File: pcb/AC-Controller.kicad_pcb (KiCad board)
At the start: 2 copper layers, 66 x 67 mm, 69 parts, among them J1 Serial, J2 USB_C_Top, J3 USB_C_Bottom, Q1 2N7002, Q2 AO3401A, SW1 Mode, SW2 Value, U1 ESP32-WROOM-32, U2 TPS63000, U3 TPS63000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

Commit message: style: schematics cleanup
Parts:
- R24, R25: value 1M -> 10M
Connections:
- net VBUS renamed /Power/V_{BUS}
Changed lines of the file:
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@@
   )
   (paper "A4")
+  (title_block
+    (title "Qeteshs AC-Controller")
+    (date "~DATE~")
+    (rev "~VERSION~")
+  )
   (layers
     (0 "F.Cu" signal)
@@
   (net 5 "/Encoder1_A")
   (net 6 "/Encoder2_A")
-  (net 7 "VBUS")
+  (net 7 "/Power/V_{BUS}")
   (net 8 "Net-(D1-A)")
   (net 9 "/LCD_VO")
@@
     (descr "Resistor SMD 0402 (1005 Metric), square (rectangular) end terminal, IPC_7351 nominal, (Body size source: IPC-SM-782 page 72, https://www.pcb-3d.com/wordpress/wp-content/uploads/ipc-sm-782a_amendment_1_and_2.pdf), generated with kicad-footprint-generator")
     (tags "resistor")
-    (property "LCSC" "C26083")
+    (property "LCSC" "C26082")
     (property "Sheetfile" "AC-Controller.kicad_sch")
     (property "Sheetname" "")
@@
         (effects (font (size 0.8 0.8) (thickness 0.15)))
     )
-    (fp_text value "1M" (at 0 1.17) (layer "F.Fab")
+    (fp_text value "10M" (at 0 1.17) (layer "F.Fab")
         (effects (font (size 1 1) (thickness 0.15)))
     )
@@
       (stroke (width 0.1) (type solid)) (layer "F.Fab"))
     (pad "1" smd roundrect (at -0.9375 -0.95 270) (size 1.475 0.6) (layers "F.Cu" "F.Paste" "F.Mask") (roundrect_rratio 0.25)
-      (net 7 "VBUS") (pinfunction "G") (pintype "input"))
+      (net 7 "/Power/V_{BUS}") (pinfunction "G") (pintype "input"))
     (pad "2" smd roundrect (at -0.9375 0.95 270) (size 1.475 0.6) (layers "F.Cu" "F.Paste" "F.Mask") (roundrect_rratio 0.25)
       (net 43 "/Power/V_{IN}") (pinfunction "S") (pintype "passive"))
@@
       (net 39 "/Power/CC1a") (pinfunction "CC1") (pintype "bidirectional"))
     (pad "A9" smd rect (at 1.52 -3.08 180) (size 0.76 1.2) (layers "F.Cu" "F.Paste" "F.Mask")
-      (net 7 "VBUS") (pinfunction "VBUS") (pintype "passive"))
+      (net 7 "/Power/V_{BUS}") (pinfunction "VBUS") (pintype "passive"))
     (pad "A12" smd rect (at 2.75 -3.08 180) (size 0.8 1.2) (layers "F.Cu" "F.Paste" "F.Mask")
       (net 1 "GND") (pinfunction "GND") (pintype "passive"))
@@
       (net 40 "/Power/CC2a") (pinfunction "CC2") (pintype "bidirectional"))
     (pad "B9" smd rect (at -1.52 -3.08 180) (size 0.76 1.2) (layers "F.Cu" "F.Paste" "F.Mask")
-      (net 7 "VBUS") (pinfunction "VBUS") (pintype "passive"))
+      (net 7 "/Power/V_{BUS}") (pinfunction "VBUS") (pintype "passive"))
     (pad "B12" smd rect (at -2.75 -3.08 180) (size 0.8 1.2) (layers "F.Cu" "F.Paste" "F.Mask")
       (net 1 "GND") (pinfunction "GND") (pintype "passive"))
@@
       (stroke (width 0.1) (type solid)) (layer "F.Fab"))
     (pad "1" smd roundrect (at -0.51 0 270) (size 0.54 0.64) (layers "F.Cu" "F.Paste" "F.Mask") (roundrect_rratio 0.25)
-      (net 7 "VBUS") (pintype "passive"))
+      (net 7 "/Power/V_{BUS}") (pintype "passive"))
     (pad "2" smd roundrect (at 0.51 0 270) (size 0.54 0.64) (layers "F.Cu" "F.Paste" "F.Mask") (roundrect_rratio 0.25)
       (net 1 "GND") (pintype "passive"))
@@
       (net 43 "/Power/V_{IN}") (pinfunction "K") (pintype "passive"))
     (pad "2" smd roundrect (at 1.05 0) (size 0.6 0.45) (layers "F.Cu" "F.Paste" "F.Mask") (roundrect_rratio 0.25)
-      (net 7 "VBUS") (pinfunction "A") (pintype "passive"))
+      (net 7 "/Power/V_{BUS}") (pinfunction "A") (pintype "passive"))
     (model "${KICAD6_3DMODEL_DIR}/Diode_SMD.3dshapes/D_SOD-323.wrl"
       (offset (xyz 0 0 0))
@@
       (net 41 "/Power/CC1b") (pinfunction "CC1") (pintype "bidirectional"))
     (pad "A9" smd rect (at 1.52 -3.08) (size 0.76 1.2) (layers "F.Cu" "F.Paste" "F.Mask")
-      (net 7 "VBUS") (pinfunction "VBUS") (pintype "passive"))
+      (net 7 "/Power/V_{BUS}") (pinfunction "VBUS") (pintype "passive"))
     (pad "A12" smd rect (at 2.75 -3.08) (size 0.8 1.2) (layers "F.Cu" "F.Paste" "F.Mask")
       (net 1 "GND") (pinfunction "GND") (pintype "passive"))
@@
       (net 42 "/Power/CC2b") (pinfunction "CC2") (pintype "bidirectional"))
     (pad "B9" smd rect (at -1.52 -3.08) (size 0.76 1.2) (layers "F.Cu" "F.Paste" "F.Mask")
-      (net 7 "VBUS") (pinfunction "VBUS") (pintype "passive"))
+      (net 7 "/Power/V_{BUS}") (pinfunction "VBUS") (pintype "passive"))
     (pad "B12" smd rect (at -2.75 -3.08) (size 0.8 1.2) (layers "F.Cu" "F.Paste" "F.Mask")
       (net 1 "GND") (pinfunction "GND") (pintype "passive"))
@@
       (net 1 "GND") (pinfunction "GND") (pintype "power_in"))
     (pad "4" smd roundrect (at -2.475 1.905) (size 1.97 0.6) (layers "F.Cu" "F.Paste" "F.Mask") (roundrect_rratio 0.07)
-      (net 7 "VBUS") (pinfunction "VCC") (pintype "power_in"))
+      (net 7 "/Power/V_{BUS}") (pinfunction "VCC") (pintype "power_in"))
     (pad "5" smd roundrect (at 2.475 1.905) (size 1.97 0.6) (layers "F.Cu" "F.Paste" "F.Mask") (roundrect_rratio 0.07)
       (net 55 "/Battery+") (pinfunction "BAT") (pintype "output"))
@@
       (net 53 "/~{Battery_Charging}") (pinfunction "~{CHRG}") (pintype "output"))
     (pad "8" smd roundrect (at 2.475 -1.905) (size 1.97 0.6) (layers "F.Cu" "F.Paste" "F.Mask") (roundrect_rratio 0.07)
-      (net 7 "VBUS") (pinfunction "CE") (pintype "input"))
+      (net 7 "/Power/V_{BUS}") (pinfunction "CE") (pintype "input"))
     (pad "9" smd rect (at 0 0) (size 2.413 3.302) (layers "F.Cu" "F.Mask")
       (net 1 "GND") (pinfunction "EP") (pintype "passive"))
@@
     (descr "Resistor SMD 0402 (1005 Metric), square (rectangular) end terminal, IPC_7351 nominal, (Body size source: IPC-SM-782 page 72, https://www.pcb-3d.com/wordpress/wp-content/uploads/ipc-sm-782a_amendment_1_and_2.pdf), generated with kicad-footprint-generator")
     (tags "resistor")
-    (property "LCSC" "C26083")
+    (property "LCSC" "C26082")
     (property "Sheetfile" "AC-Controller.kicad_sch")
     (property "Sheetname" "")
@@
         (effects (font (size 0.8 0.8) (thickness 0.15)))
     )
-    (fp_text value "1M" (at 0 3.17) (layer "F.Fab")
+    (fp_text value "10M" (at 0 3.17) (layer "F.Fab")
         (effects (font (size 1 1) (thickness 0.15)))
     )
@@
     )
   )
-  (zone (net 7) (net_name "VBUS") (layer "B.Cu") (name "VBUS") (hatch edge 0.5)
+  (zone (net 7) (net_name "/Power/V_{BUS}") (layer "B.Cu") (name "VBUS") (hatch edge 0.5)
     (priority 10)
     (connect_pads (clearance 0.25))

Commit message: style: use correct variables
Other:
- board text added: "${VERSION} ${DATE}"
- board text removed: "~VERSION~ ~DATE~"
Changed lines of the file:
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@@
   (title_block
     (title "Qeteshs AC-Controller")
-    (date "~DATE~")
-    (rev "~VERSION~")
+    (date "${DATE}")
+    (rev "${VERSION}")
   )
   (layers
@@
     (effects (font (size 1 1) (thickness 0.15)) (justify bottom mirror))
   )
-  (gr_text "~VERSION~\n~DATE~" (at 150 95.75) (layer "B.SilkS")
+  (gr_text "${VERSION}\n${DATE}" (at 150 95.75) (layer "B.SilkS")
     (effects (font (size 1 1) (thickness 0.15)) (justify mirror))
   )
@@
     (effects (font (size 1 1) (thickness 0.15)) (justify right mirror))
   )
-  (gr_text "~VERSION~\n~DATE~" (at 150 66.75) (layer "F.SilkS")
+  (gr_text "${VERSION}\n${DATE}" (at 150 66.75) (layer "F.SilkS")
     (effects (font (size 1 1) (thickness 0.15)))
   )

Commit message: style: add 3d models for pcb render
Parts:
- L1, L2: value 3.3uH -> DR74-3R3-R
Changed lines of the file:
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@@
         (effects (font (size 0.8 0.8) (thickness 0.15)))
     )
-    (fp_text value "3.3uH" (at 0 -4.75 unlocked) (layer "F.Fab")
+    (fp_text value "DR74-3R3-R" (at 0 -4.75 unlocked) (layer "F.Fab")
         (effects (font (size 1 1) (thickness 0.15)))
     )
@@
     (pad "2" smd roundrect (at 3.2 0 90) (size 3.25 3) (property pad_prop_heatsink) (layers "F.Cu" "F.Paste" "F.Mask") (roundrect_rratio 0.25)
       (net 47 "Net-(U2-L1)") (pintype "passive") (thermal_bridge_width 0.5) (thermal_bridge_angle 45))
+    (model ":KICAD7_3DMODEL_DIR:Inductor_SMD.3dshapes/L_Bourns_SRR1260.step"
+      (offset (xyz 0 0 0))
+      (scale (xyz 0.6 0.6 0.5))
+      (rotate (xyz 0 0 0))
+    )
   )
   (footprint "Resistor_SMD:R_0603_1608Metric" (layer "F.Cu")
@@
           (width 0) (fill yes))
       ))
-    (model "${KICAD6_3DMODEL_DIR}/Package_SON.3dshapes/Texas_DRC0010J.wrl"
+    (model ":KICAD7_3DMODEL_DIR:Package_SON.3dshapes/Texas_S-PVSON-N10.step"
       (offset (xyz 0 0 0))
       (scale (xyz 1 1 1))
@@
           (width 0) (fill yes))
       ))
-    (model "${KICAD6_3DMODEL_DIR}/Package_SON.3dshapes/Texas_DRC0010J.wrl"
+    (model ":KICAD7_3DMODEL_DIR:Package_SON.3dshapes/Texas_S-PVSON-N10.step"
       (offset (xyz 0 0 0))
       (scale (xyz 1 1 1))
@@
         (effects (font (size 0.8 0.8) (thickness 0.15)))
     )
-    (fp_text value "3.3uH" (at 0 -4.75 90 unlocked) (layer "F.Fab")
+    (fp_text value "DR74-3R3-R" (at 0 -4.75 90 unlocked) (layer "F.Fab")
         (effects (font (size 1 1) (thickness 0.15)))
     )
@@
     (pad "2" smd roundrect (at 3.2 0 180) (size 3.25 3) (property pad_prop_heatsink) (layers "F.Cu" "F.Paste" "F.Mask") (roundrect_rratio 0.25)
       (net 49 "Net-(U3-L1)") (pintype "passive") (thermal_bridge_angle 45))
+    (model ":KICAD7_3DMODEL_DIR:Inductor_SMD.3dshapes/L_Bourns_SRR1260.step"
+      (offset (xyz 0 0 0))
+      (scale (xyz 0.6 0.6 0.5))
+      (rotate (xyz 0 0 0))
+    )
   )
   (footprint "Package_TO_SOT_SMD:SOT-23" (layer "F.Cu")
@@
     (pad "9" smd rect (at 0 0) (size 2.413 3.302) (layers "F.Cu" "F.Mask")
       (net 1 "GND") (pinfunction "EP") (pintype "passive"))
+    (model ":KICAD7_3DMODEL_DIR:Package_SO.3dshapes/HTSOP-8-1EP_3.9x4.9mm_Pitch1.27mm.step"
+      (offset (xyz 0 0 0))
+      (scale (xyz 1 1 1))
+      (rotate (xyz 0 0 0))
+    )
   )
   (footprint "Capacitor_SMD:C_0603_1608Metric" (layer "F.Cu")

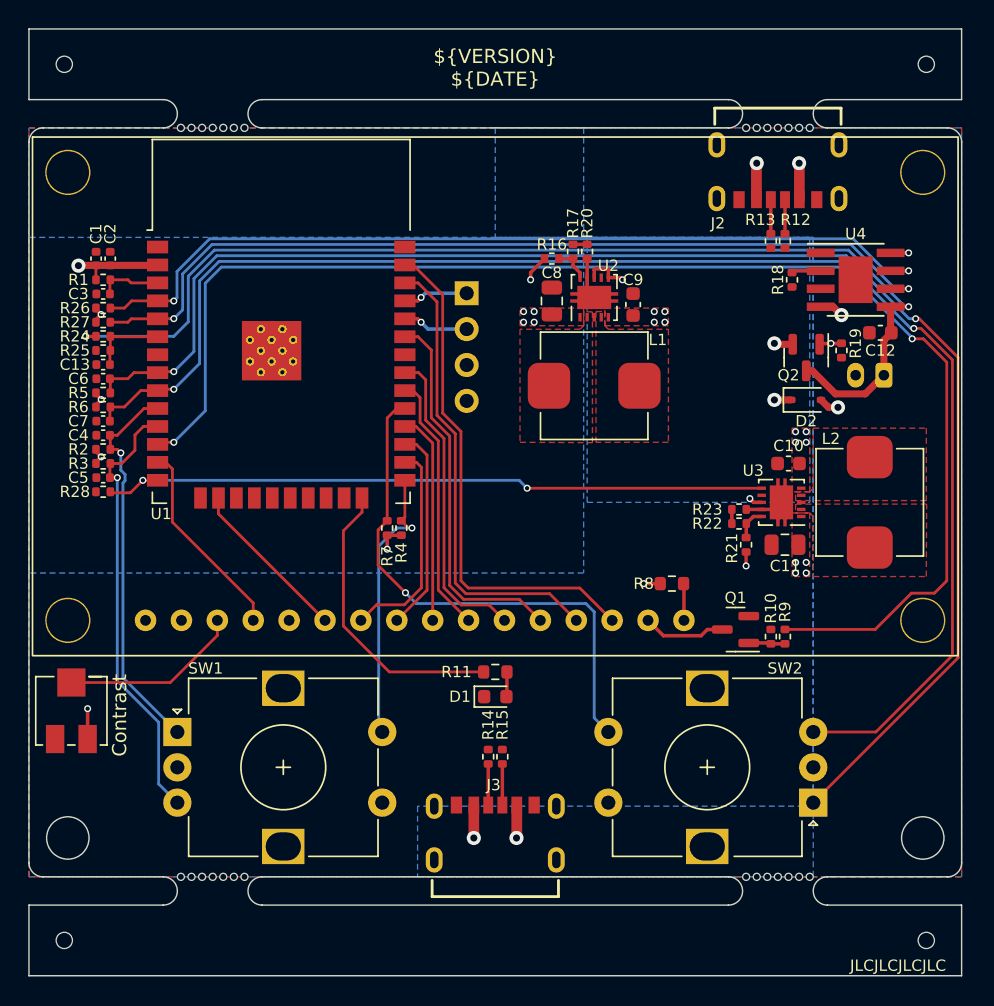
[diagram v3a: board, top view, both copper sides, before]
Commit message: feat: add battery protection
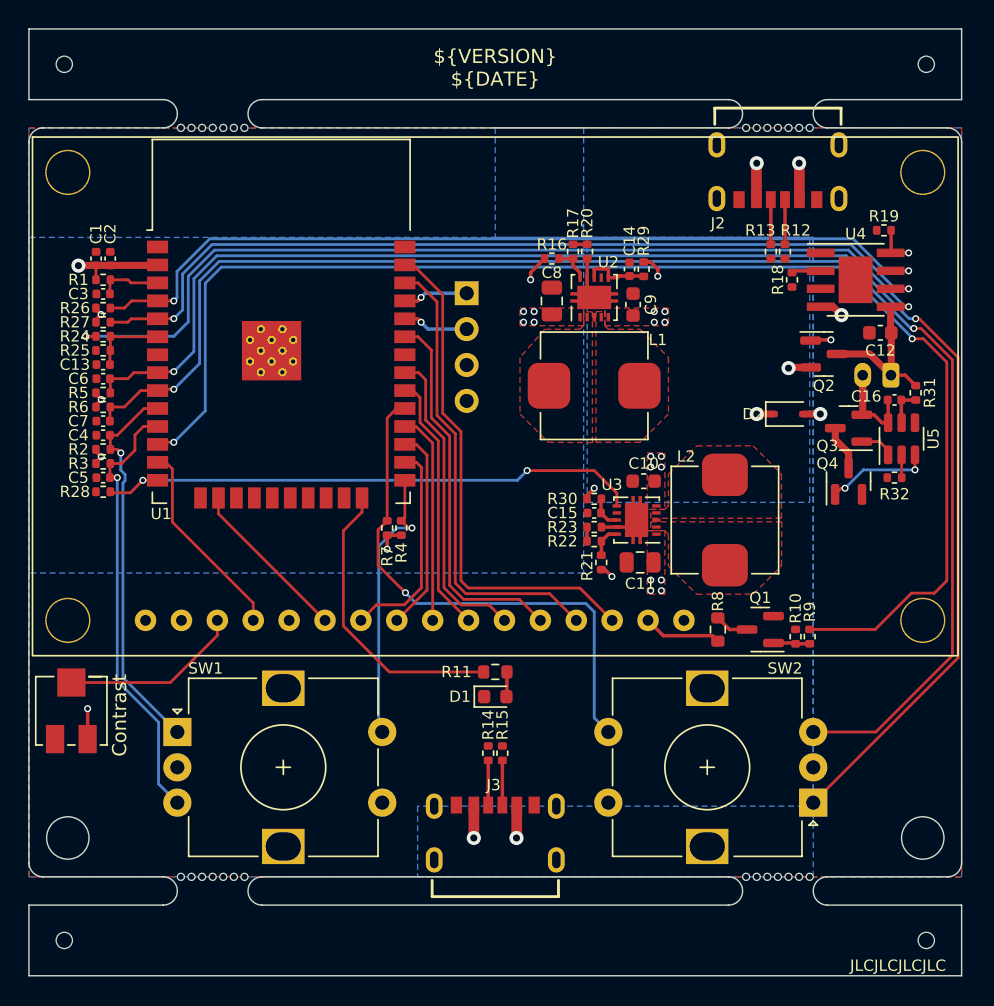
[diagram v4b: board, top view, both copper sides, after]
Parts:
- added C14: 100n, Capacitor_SMD:C_0402_1005Metric, F.Cu at (159.5, 81.0)
- added C15: 100n, Capacitor_SMD:C_0402_1005Metric, F.Cu at (157.0, 98.2)
- added C16: 100n, Capacitor_SMD:C_0402_1005Metric, F.Cu at (178.2, 90.2)
- added Q3: AO3400A, Package_TO_SOT_SMD:SOT-23, F.Cu at (175.0, 92.2)
- added Q4: AO3400A, Package_TO_SOT_SMD:SOT-23, F.Cu at (175.0, 96.0)
- added R29: 100R, Resistor_SMD:R_0402_1005Metric, F.Cu at (160.5, 81.0)
- added R30: 100R, Resistor_SMD:R_0402_1005Metric, F.Cu at (157.0, 97.2)
- added R31: 100R, Resistor_SMD:R_0402_1005Metric, F.Cu at (179.8, 89.8)
- added R32: 1k, Resistor_SMD:R_0402_1005Metric, F.Cu at (178.2, 95.8)
- added U5: DW01A, Package_TO_SOT_SMD:SOT-23-6, F.Cu at (178.8, 93.0)
- Q1: value 2N7002 -> AO3400A
- R18: value 10k -> 2k
- R8: value 0R -> 20R
- moved C10 10.3 mm to (160.5, 96.0)
- moved C11 10.3 mm to (160.2, 101.8)
- moved L2 10.3 mm to (166.2, 98.8)
- moved R21 10.3 mm to (157.5, 101.8)
- moved R22 10.3 mm to (157.0, 100.2)
- moved R23 10.3 mm to (157.0, 99.2)
- moved U3 10.3 mm to (160.0, 98.8)
- moved R19 9.01 mm to (177.5, 78.2), turned to 180 degrees
- moved R8 4.60 mm to (165.8, 106.5), turned to 90 degrees
- moved Q1 1.75 mm to (168.8, 106.5)
- moved R10 1.75 mm to (171.2, 107.0)
- moved R9 1.75 mm to (172.2, 107.0)
- moved D2 1.60 mm to (170.8, 91.2)
- moved Q2 1.27 mm to (173.2, 87.0), turned to 0 degrees
- moved R12 0.75 mm to (170.5, 79.8)
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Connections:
- BT1 pad 2: GND -> /Power/Battery-
- DS1 pad 16: /LCD_LED_A -> +5V
- Q1 pad 3: /LCD_LED_K -> Net-(Q1-D)
- R8 pad 1: /LCD_LED_A -> /LCD_LED_K
- R8 pad 2: +5V -> Net-(Q1-D)
- U2 pad 6: /Power/V_{IN} -> /Power/VINA3
- U2 pad 8: /Power/V_{IN} -> /Power/VINA3
- U3 pad 8: /Power/V_{IN} -> /Power/VINA5
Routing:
- net /5VEN: track 47.8 -> 39.1 mm
- net /Power/OC: track 0.00 -> 7.43 mm, vias 0 -> 2
- net /Power/Battery-: track 0.00 -> 6.55 mm
- net /Power/VINA3: track 0.00 -> 4.75 mm
- net Net-(Q3-D): track 0.00 -> 3.20 mm
- net Net-(U5-VCC): track 0.00 -> 2.64 mm
- net /LCD_LED_A: track 2.61 -> 0.00 mm
- net /Power/OD: track 0.00 -> 2.45 mm
- net Net-(Q1-D): track 0.00 -> 2.40 mm
- net /Power/VINA5: track 0.00 -> 2.34 mm
- net /LCD_BL: track 97.5 -> 95.8 mm
- net /Power/VM: track 0.00 -> 1.62 mm
- net /Power/V_{BUS}: track 15.8 -> 17.1 mm
- net /Power/V_{IN}: track 6.72 -> 5.46 mm
- net +5V: track 4.32 -> 3.10 mm, vias 7 -> 6
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
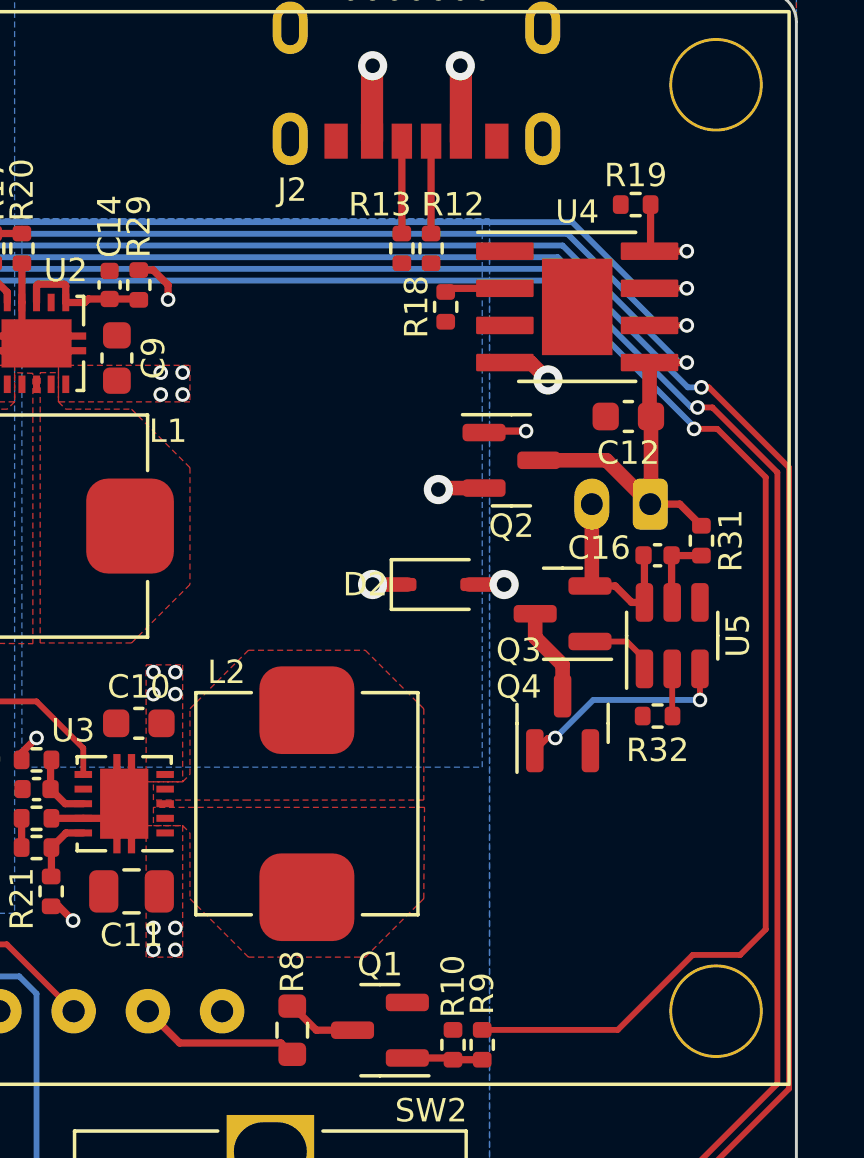
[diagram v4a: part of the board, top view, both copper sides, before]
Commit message: feat: add reverse polarity protection for battery input
just to make sure a reverse connected battery won't kill the circuit
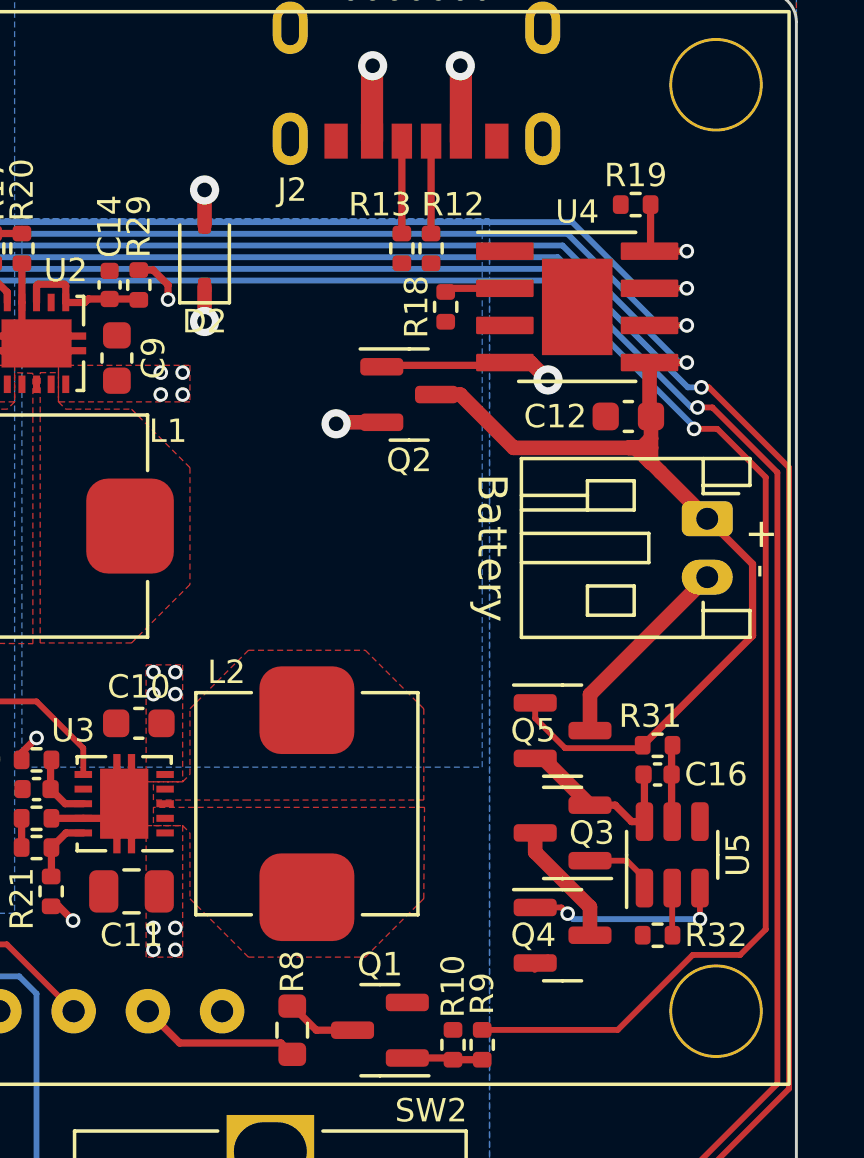
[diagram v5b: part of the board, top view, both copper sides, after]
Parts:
- added Q5: AO3400A, Package_TO_SOT_SMD:SOT-23, F.Cu at (175.0, 96.2)
- BT1: moved to F.Cu
- moved D2 13.8 mm to (162.8, 80.0), turned to 90 degrees
- moved C16 7.50 mm to (178.2, 97.8)
- moved Q3 7.50 mm to (175.0, 99.8)
- moved R32 7.50 mm to (178.2, 103.2)
- moved U5 7.50 mm to (178.8, 100.5)
- moved Q4 7.25 mm to (175.0, 103.2), turned to 0 degrees
- moved R31 7.16 mm to (178.2, 96.8), turned to 180 degrees
- moved Q2 4.16 mm to (169.8, 84.8)
- moved BT1 2.01 mm to (179.9, 89.0), turned to -90 degrees
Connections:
- BT1 pad 2: /Power/Battery- -> /Power/B-
- C16 pad 1: /Power/Battery- -> /Power/B_{GND}
- Q3 pad 2: /Power/Battery- -> /Power/B_{GND}
- U5 pad 6: /Power/Battery- -> /Power/B_{GND}
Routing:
- net /Battery+: track 77.7 -> 97.4 mm
- net /Power/B-: track 0.00 -> 6.91 mm
- net /Power/Battery-: track 6.55 -> 0.00 mm
- net /Power/B_{GND}: track 0.00 -> 6.26 mm
- net /Power/V_{BUS}: track 17.1 -> 19.9 mm, vias 8 -> 7
- net Net-(Q3-D): track 3.20 -> 4.28 mm
- net GND: track 6.35 -> 6.97 mm
- net /Power/OC: track 7.43 -> 6.87 mm
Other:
- board text added: "+ -"
- board text added: "Battery"
- board text removed: "Battery + -"
